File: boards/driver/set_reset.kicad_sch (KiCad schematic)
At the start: 22 parts, among them Q39 MMBT2222, Q40 MMBT2907, Q41 MMBT2222, Q42 MMBT2222

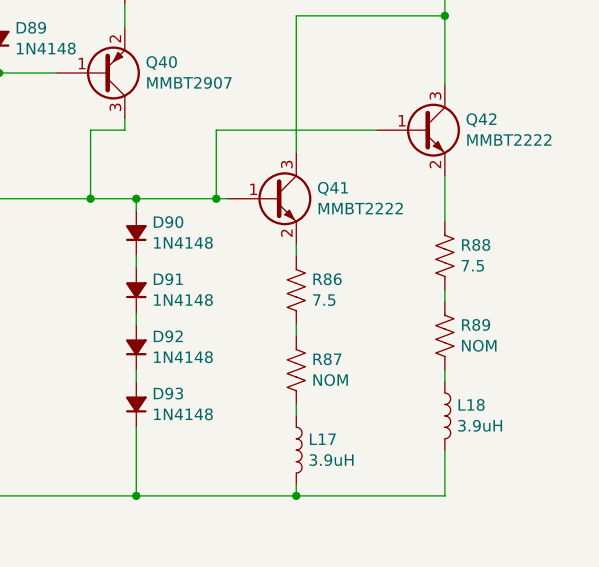
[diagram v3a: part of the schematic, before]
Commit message: Driver: filled out the rest of the BOM, except for defaults for nominal resistances
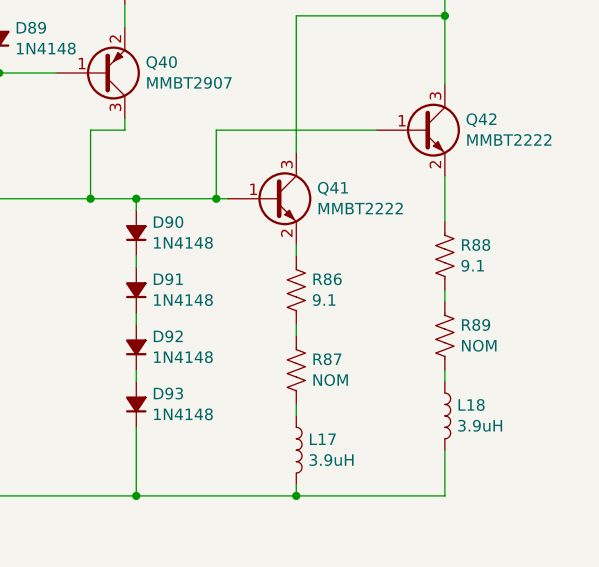
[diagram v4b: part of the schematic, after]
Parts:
- R81, R82: MPN (none) -> ESR03EZPF1001; Manufacturer (none) -> Rohm Semiconductor; Package (none) -> 0603; Rating (none) -> 1/4W; Tolerance (none) -> 1%
- R83, R84: MPN (none) -> ERJ-UP3F5101V; Manufacturer (none) -> Panasonic Electronic Components; Package (none) -> 0603; Rating (none) -> 1/4W; Tolerance (none) -> 1%
- R85: MPN (none) -> ERJ-PA3F27R0V; Manufacturer (none) -> Panasonic Electronic Components; Package (none) -> 0603; Rating (none) -> 1/3W; Tolerance (none) -> 1%
- R86, R88: value 7.5 -> 9.1; MPN (none) -> ESR10EZPF9R10; Manufacturer (none) -> Rohm Semiconductor; Package (none) -> 0805; Rating (none) -> 2/5W; Tolerance (none) -> 1%
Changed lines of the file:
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@@
+      (effects (font (size 1.27 1.27)) hide)
+    )
+    (property "Description" "RES SMD 1K OHM PULSE-WITHSTANDING 1% 1/4W 0603" (id 4) (at 101.6 90.17 0)
+      (effects (font (size 1.27 1.27)) hide)
+    )
+    (property "MPN" "ESR03EZPF1001" (id 5) (at 101.6 90.17 0)
+      (effects (font (size 1.27 1.27)) hide)
+    )
+    (property "Manufacturer" "Rohm Semiconductor" (id 6) (at 101.6 90.17 0)
+      (effects (font (size 1.27 1.27)) hide)
+    )
+    (property "Package" "0603" (id 7) (at 101.6 90.17 0)
+      (effects (font (size 1.27 1.27)) hide)
+    )
+    (property "Rating" "1/4W" (id 8) (at 101.6 90.17 0)
+      (effects (font (size 1.27 1.27)) hide)
+    )
+    (property "Tolerance" "1%" (id 9) (at 101.6 90.17 0)
       (effects (font (size 1.27 1.27)) hide)
     )
@@
       (effects (font (size 1.27 1.27)) hide)
     )
+    (property "Description" "RES SMD 1K OHM PULSE-WITHSTANDING 1% 1/4W 0603" (id 4) (at 121.92 83.82 0)
+      (effects (font (size 1.27 1.27)) hide)
+    )
+    (property "MPN" "ESR03EZPF1001" (id 5) (at 121.92 83.82 0)
+      (effects (font (size 1.27 1.27)) hide)
+    )
+    (property "Manufacturer" "Rohm Semiconductor" (id 6) (at 121.92 83.82 0)
+      (effects (font (size 1.27 1.27)) hide)
+    )
+    (property "Package" "0603" (id 7) (at 121.92 83.82 0)
+      (effects (font (size 1.27 1.27)) hide)
+    )
+    (property "Rating" "1/4W" (id 8) (at 121.92 83.82 0)
+      (effects (font (size 1.27 1.27)) hide)
+    )
+    (property "Tolerance" "1%" (id 9) (at 121.92 83.82 0)
+      (effects (font (size 1.27 1.27)) hide)
+    )
     (pin "1")
     (pin "2")
@@
       (effects (font (size 1.27 1.27)) hide)
     )
+    (property "Description" "RES 5.1K OHM PULSE-WITHSTANDING 1% 1/4W 0603" (id 4) (at 127 73.66 0)
+      (effects (font (size 1.27 1.27)) hide)
+    )
+    (property "MPN" "ERJ-UP3F5101V" (id 5) (at 127 73.66 0)
+      (effects (font (size 1.27 1.27)) hide)
+    )
+    (property "Manufacturer" "Panasonic Electronic Components" (id 6) (at 127 73.66 0)
+      (effects (font (size 1.27 1.27)) hide)
+    )
+    (property "Package" "0603" (id 7) (at 127 73.66 0)
+      (effects (font (size 1.27 1.27)) hide)
+    )
+    (property "Rating" "1/4W" (id 8) (at 127 73.66 0)
+      (effects (font (size 1.27 1.27)) hide)
+    )
+    (property "Tolerance" "1%" (id 9) (at 127 73.66 0)
+      (effects (font (size 1.27 1.27)) hide)
+    )
     (pin "1")
     (pin "2")
@@
       (effects (font (size 1.27 1.27)) hide)
     )
+    (property "Description" "RES SMD 27 OHM PULSE-WITHSTANDING 1% 1/3W 0603" (id 4) (at 149.86 72.39 0)
+      (effects (font (size 1.27 1.27)) hide)
+    )
+    (property "MPN" "ERJ-PA3F27R0V" (id 5) (at 149.86 72.39 0)
+      (effects (font (size 1.27 1.27)) hide)
+    )
+    (property "Manufacturer" "Panasonic Electronic Components" (id 6) (at 149.86 72.39 0)
+      (effects (font (size 1.27 1.27)) hide)
+    )
+    (property "Package" "0603" (id 7) (at 149.86 72.39 0)
+      (effects (font (size 1.27 1.27)) hide)
+    )
+    (property "Rating" "1/3W" (id 8) (at 149.86 72.39 0)
+      (effects (font (size 1.27 1.27)) hide)
+    )
+    (property "Tolerance" "1%" (id 9) (at 149.86 72.39 0)
+      (effects (font (size 1.27 1.27)) hide)
+    )
     (pin "1")
     (pin "2")
@@
     )
     (property "Datasheet" "~" (id 3) (at 128.27 105.41 0)
+      (effects (font (size 1.27 1.27)) hide)
+    )
+    (property "Description" "RES 5.1K OHM PULSE-WITHSTANDING 1% 1/4W 0603" (id 4) (at 128.27 105.41 0)
+      (effects (font (size 1.27 1.27)) hide)
+    )
+    (property "MPN" "ERJ-UP3F5101V" (id 5) (at 128.27 105.41 0)
+      (effects (font (size 1.27 1.27)) hide)
+    )
+    (property "Manufacturer" "Panasonic Electronic Components" (id 6) (at 128.27 105.41 0)
+      (effects (font (size 1.27 1.27)) hide)
+    )
+    (property "Package" "0603" (id 7) (at 128.27 105.41 0)
+      (effects (font (size 1.27 1.27)) hide)
+    )
+    (property "Rating" "1/4W" (id 8) (at 128.27 105.41 0)
+      (effects (font (size 1.27 1.27)) hide)
+    )
+    (property "Tolerance" "1%" (id 9) (at 128.27 105.41 0)
       (effects (font (size 1.27 1.27)) hide)
     )
@@
       (effects (font (size 1.27 1.27)) (justify left))
     )
-    (property "Value" "7.5" (id 1) (at 170.6372 109.093 0)
+    (property "Value" "9.1" (id 1) (at 170.6372 109.093 0)
       (effects (font (size 1.27 1.27)) (justify left))
     )
@@
       (effects (font (size 1.27 1.27)) hide)
     )
+    (property "Description" "RES SMD 9.1 OHM PULSE-WITHSTANDING 1% 0.4W 0805" (id 4) (at 168.91 107.95 0)
+      (effects (font (size 1.27 1.27)) hide)
+    )
+    (property "MPN" "ESR10EZPF9R10" (id 5) (at 168.91 107.95 0)
+      (effects (font (size 1.27 1.27)) hide)
+    )
+    (property "Manufacturer" "Rohm Semiconductor" (id 6) (at 168.91 107.95 0)
+      (effects (font (size 1.27 1.27)) hide)
+    )
+    (property "Package" "0805" (id 7) (at 168.91 107.95 0)
+      (effects (font (size 1.27 1.27)) hide)
+    )
+    (property "Rating" "2/5W" (id 8) (at 168.91 107.95 0)
+      (effects (font (size 1.27 1.27)) hide)
+    )
+    (property "Tolerance" "1%" (id 9) (at 168.91 107.95 0)
+      (effects (font (size 1.27 1.27)) hide)
+    )
     (pin "1")
     (pin "2")
@@
       (effects (font (size 1.27 1.27)) (justify left))
     )
-    (property "Value" "7.5" (id 1) (at 187.1472 105.283 0)
+    (property "Value" "9.1" (id 1) (at 187.1472 105.283 0)
       (effects (font (size 1.27 1.27)) (justify left))
     )
@@
       (effects (font (size 1.27 1.27)) hide)
     )
+    (property "Description" "RES SMD 9.1 OHM PULSE-WITHSTANDING 1% 0.4W 0805" (id 4) (at 185.42 104.14 0)
+      (effects (font (size 1.27 1.27)) hide)
+    )
+    (property "MPN" "ESR10EZPF9R10" (id 5) (at 185.42 104.14 0)
+      (effects (font (size 1.27 1.27)) hide)
+    )
+    (property "Manufacturer" "Rohm Semiconductor" (id 6) (at 185.42 104.14 0)
+      (effects (font (size 1.27 1.27)) hide)
+    )
+    (property "Package" "0805" (id 7) (at 185.42 104.14 0)
+      (effects (font (size 1.27 1.27)) hide)
+    )
+    (property "Rating" "2/5W" (id 8) (at 185.42 104.14 0)
+      (effects (font (size 1.27 1.27)) hide)
+    )
+    (property "Tolerance" "1%" (id 9) (at 185.42 104.14 0)
+      (effects (font (size 1.27 1.27)) hide)
+    )

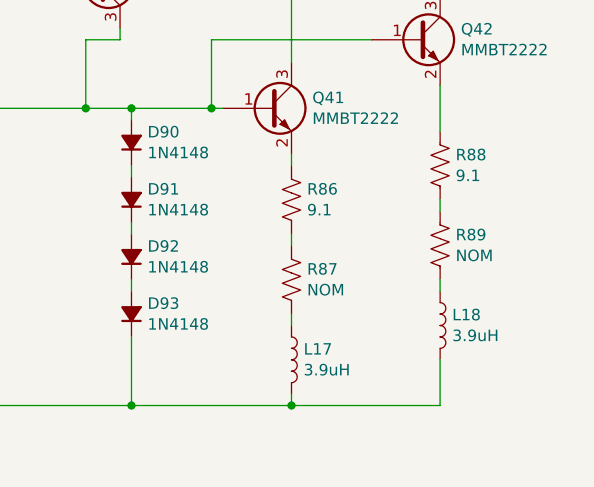
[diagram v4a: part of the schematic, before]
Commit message: Driver: completed the BOM and added some reference dimensions to the board layout
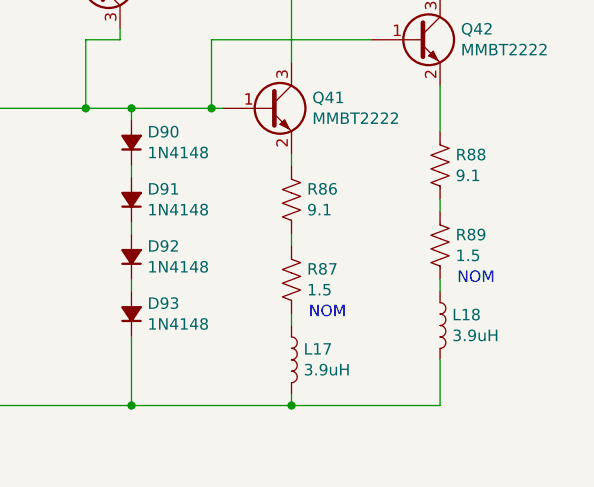
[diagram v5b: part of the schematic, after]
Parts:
- R87, R89: value NOM -> 1.5; MPN (none) -> RCS06031R50FKEA; Manufacturer (none) -> Vishay Dale; Package (none) -> 0603; Rating (none) -> 1/4W; Tolerance (none) -> 1%
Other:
- note added: "NOM"
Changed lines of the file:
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@@
     (stroke (width 0) (type default) (color 0 0 0 0))
+  )
+  (text "NOM" (at 187.325 117.475 0)
+    (effects (font (size 1.27 1.27)) (justify left bottom))
+  )
+  (text "NOM" (at 170.815 121.285 0)
+    (effects (font (size 1.27 1.27)) (justify left bottom))
   )
   (hierarchical_label "BPLIZ" (shape input) (at 100.33 63.5 180)
@@
       (effects (font (size 1.27 1.27)) (justify left))
     )
-    (property "Value" "NOM" (id 1) (at 170.6372 117.983 0)
+    (property "Value" "1.5" (id 1) (at 170.6372 117.983 0)
       (effects (font (size 1.27 1.27)) (justify left))
     )
@@
       (effects (font (size 1.27 1.27)) hide)
     )
+    (property "Description" "RES SMD 1.5 OHM PULSE-WITHSTANDING  1% 1/4W 0603" (id 4) (at 168.91 116.84 0)
+      (effects (font (size 1.27 1.27)) hide)
+    )
+    (property "MPN" "RCS06031R50FKEA" (id 5) (at 168.91 116.84 0)
+      (effects (font (size 1.27 1.27)) hide)
+    )
+    (property "Manufacturer" "Vishay Dale" (id 6) (at 168.91 116.84 0)
+      (effects (font (size 1.27 1.27)) hide)
+    )
+    (property "Package" "0603" (id 7) (at 168.91 116.84 0)
+      (effects (font (size 1.27 1.27)) hide)
+    )
+    (property "Rating" "1/4W" (id 8) (at 168.91 116.84 0)
+      (effects (font (size 1.27 1.27)) hide)
+    )
+    (property "Tolerance" "1%" (id 9) (at 168.91 116.84 0)
+      (effects (font (size 1.27 1.27)) hide)
+    )
     (pin "1")
     (pin "2")
@@
       (effects (font (size 1.27 1.27)) (justify left))
     )
-    (property "Value" "NOM" (id 1) (at 187.1472 114.173 0)
+    (property "Value" "1.5" (id 1) (at 187.1472 114.173 0)
       (effects (font (size 1.27 1.27)) (justify left))
     )
@@
       (effects (font (size 1.27 1.27)) hide)
     )
+    (property "Description" "RES SMD 1.5 OHM PULSE-WITHSTANDING  1% 1/4W 0603" (id 4) (at 185.42 113.03 0)
+      (effects (font (size 1.27 1.27)) hide)
+    )
+    (property "MPN" "RCS06031R50FKEA" (id 5) (at 185.42 113.03 0)
+      (effects (font (size 1.27 1.27)) hide)
+    )
+    (property "Manufacturer" "Vishay Dale" (id 6) (at 185.42 113.03 0)
+      (effects (font (size 1.27 1.27)) hide)
+    )
+    (property "Package" "0603" (id 7) (at 185.42 113.03 0)
+      (effects (font (size 1.27 1.27)) hide)
+    )
+    (property "Rating" "1/4W" (id 8) (at 185.42 113.03 0)
+      (effects (font (size 1.27 1.27)) hide)
+    )
+    (property "Tolerance" "1%" (id 9) (at 185.42 113.03 0)
+      (effects (font (size 1.27 1.27)) hide)
+    )
